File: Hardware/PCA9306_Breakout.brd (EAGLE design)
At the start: 17.8 x 10.2 mm, 15 parts

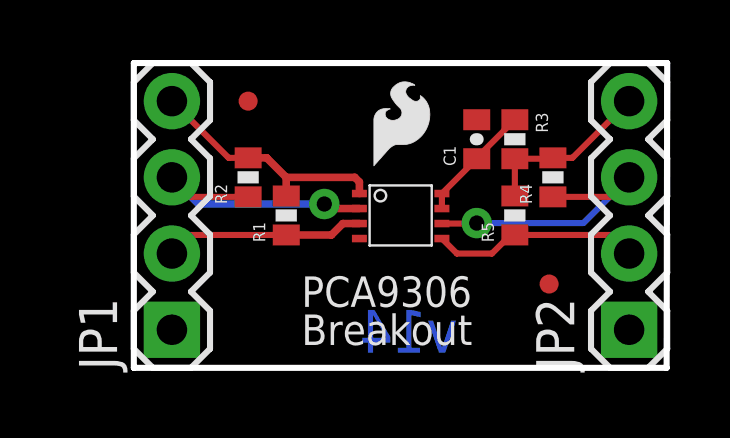
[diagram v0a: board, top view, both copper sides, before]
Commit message: Rerouted traces away from IC and changed packages to 0603. Add labels to the schematic on the header pins.
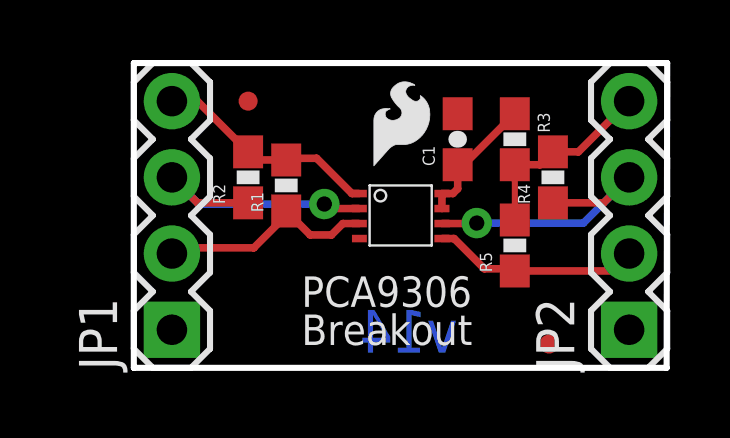
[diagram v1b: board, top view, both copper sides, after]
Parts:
- C1: device SparkFun:0402-CAP -> SparkFun:0603-CAP
- R1, R2, R3, R4, R5: device SparkFun:0402-RES -> SparkFun:0603-RES
- moved JP8 2.00 mm to (13.8, 0.79)
- moved FRAME1 1.80 mm to (-4.94, -10.2)
- moved R1 1.00 mm to (5.08, 6.08)
- moved R5 1.00 mm to (12.7, 4.08)
- moved C1 0.63 mm to (10.8, 7.62)
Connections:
- new net VREF_2: JP2.4, R3.2, R4.2, R5.2
- net VREF2: no longer JP2.4, R3.2, R4.2, R5.2
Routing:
- net VREF_2: track 0.00 -> 6.53 mm
- net VREF2: track 9.81 -> 4.50 mm
- net SDA2: track 7.84 -> 6.93 mm
- net VREF1: track 8.37 -> 7.57 mm
- net SDA1: track 6.66 -> 7.41 mm
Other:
- board text added: "T. Klopfenstein"
- board text removed: "M. Hord, T. Klopfenstein"

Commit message: Updating layout
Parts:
- moved R5 1.91 mm to (14.6, 4.08)
- moved R4 1.42 mm to (14.6, 7.62)
- moved R2 0.57 mm to (3.30, 6.10)
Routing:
- net GND: track 0.00 -> 7.88 mm
- net VREF2: track 4.50 -> 5.61 mm
- net SCL2: track 9.77 -> 8.96 mm
- net VREF_2: track 6.53 -> 7.34 mm
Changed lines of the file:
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@@
 <wire x1="0" y1="10.16" x2="0" y2="0" width="0.2032" layer="20"/>
 <wire x1="2.794" y1="11.049" x2="2.794" y2="-2.286" width="0.0254" layer="22"/>
-<wire x1="14.986" y1="11.557" x2="14.986" y2="-1.778" width="0.0254" layer="22"/>
+<wire x1="14.986" y1="10.922" x2="14.986" y2="-2.413" width="0.0254" layer="22"/>
 <wire x1="1.27" y1="8.89" x2="1.27" y2="1.27" width="0.254" layer="49"/>
 <wire x1="16.51" y1="8.89" x2="16.51" y2="1.27" width="0.254" layer="49"/>
@@
 <text x="10.795" y="0.508" size="1.4224" layer="16" font="vector" ratio="15" rot="MR0">v14</text>
 <text x="25.4" y="-10.16" size="1.778" layer="27" font="vector" ratio="15">T. Klopfenstein</text>
+<rectangle x1="7.3025" y1="3.81" x2="7.62" y2="4.1275" layer="41"/>
 </plain>
 <attributes>
@@
 <element name="U$1" library="miscellany" package="PSOP-8" value="PCA9306" x="8.89" y="5.08" rot="R270"/>
 <element name="R1" library="SparkFun" package="0603-RES" value="1k" x="5.08" y="6.08" rot="R90"/>
-<element name="R2" library="SparkFun" package="0603-RES" value="1k" x="3.81" y="6.35" rot="R90"/>
+<element name="R2" library="SparkFun" package="0603-RES" value="1k" x="3.302" y="6.096" rot="R90"/>
 <element name="R3" library="SparkFun" package="0603-RES" value="200k" x="12.7" y="7.62" rot="R270"/>
-<element name="R4" library="SparkFun" package="0603-RES" value="1k" x="13.97" y="6.35" rot="R90"/>
-<element name="R5" library="SparkFun" package="0603-RES" value="1k" x="12.7" y="4.08" rot="R90"/>
+<element name="R4" library="SparkFun" package="0603-RES" value="1k" x="14.605" y="7.62" rot="R90"/>
+<element name="R5" library="SparkFun" package="0603-RES" value="1k" x="14.605" y="4.08" rot="R90"/>
 <element name="C1" library="SparkFun" package="0603-CAP" value="0.1uF" x="10.795" y="7.62" rot="R90"/>
 <element name="JP1" library="SparkFun" package="1X04" value="" x="1.27" y="1.27" rot="R90"/>
@@
 <contactref element="JP1" pad="4"/>
 <wire x1="1.27" y1="8.89" x2="2.12" y2="8.89" width="0.254" layer="1"/>
-<wire x1="2.12" y1="8.89" x2="3.81" y2="7.2" width="0.254" layer="1"/>
+<wire x1="2.12" y1="8.89" x2="3.302" y2="6.946" width="0.254" layer="1"/>
 <wire x1="5.08" y1="6.93" x2="4.08" y2="6.93" width="0.254" layer="1"/>
-<wire x1="4.08" y1="6.93" x2="3.81" y2="7.2" width="0.254" layer="1"/>
+<wire x1="4.08" y1="6.93" x2="3.302" y2="6.946" width="0.254" layer="1"/>
 <wire x1="7.52" y1="5.81" x2="7.271" y2="5.81" width="0.254" layer="1"/>
 <wire x1="7.271" y1="5.81" x2="6.096" y2="6.985" width="0.254" layer="1"/>
@@
 <wire x1="1.27" y1="6.35" x2="2.159" y2="5.461" width="0.254" layer="16"/>
 <via x="6.35" y="5.461" extent="1-16" drill="0.508"/>
-<wire x1="3.81" y1="5.5" x2="2.12" y2="5.5" width="0.254" layer="1"/>
-<wire x1="2.12" y1="5.5" x2="1.27" y2="6.35" width="0.254" layer="1"/>
+<wire x1="3.302" y1="5.246" x2="2.374" y2="5.246" width="0.254" layer="1"/>
+<wire x1="2.374" y1="5.246" x2="1.27" y2="6.35" width="0.254" layer="1"/>
 </signal>
 <signal name="SDA1">
@@
 <vertex x="0" y="0"/>
 </polygon>
+<wire x1="7.52" y1="4.31" x2="7.1675" y2="4.31" width="0.254" layer="1"/>
+<wire x1="7.1675" y1="4.31" x2="6.6675" y2="3.81" width="0.254" layer="1"/>
+<wire x1="6.6675" y1="3.81" x2="6.35" y2="3.81" width="0.254" layer="1"/>
+<wire x1="6.35" y1="3.81" x2="6.35" y2="3.175" width="0.254" layer="1"/>
+<wire x1="6.35" y1="3.175" x2="4.445" y2="1.27" width="0.254" layer="1"/>
+<wire x1="4.445" y1="1.27" x2="1.27" y2="1.27" width="0.254" layer="1"/>
 </signal>
 <signal name="VREF2">
@@
 <wire x1="11" y1="6.77" x2="12.7" y2="8.47" width="0.254" layer="1"/>
 <contactref element="U$1" pad="8"/>
-<wire x1="10.27" y1="5.81" x2="10.27" y2="5.31" width="0.254" layer="1"/>
-<wire x1="10.27" y1="5.81" x2="10.636" y2="5.81" width="0.254" layer="1"/>
-<wire x1="10.636" y1="5.81" x2="10.795" y2="5.969" width="0.254" layer="1"/>
-<wire x1="10.795" y1="5.969" x2="10.795" y2="6.77" width="0.254" layer="1"/>
+<wire x1="10.27" y1="5.81" x2="10.954" y2="5.81" width="0.254" layer="1"/>
+<wire x1="10.27" y1="5.31" x2="10.771" y2="5.31" width="0.254" layer="1"/>
+<wire x1="10.771" y1="5.31" x2="11.049" y2="5.588" width="0.254" layer="1"/>
+<wire x1="11.049" y1="5.588" x2="11.049" y2="5.715" width="0.254" layer="1"/>
+<wire x1="11.049" y1="5.715" x2="11.049" y2="6.516" width="0.254" layer="1"/>
+<wire x1="11.049" y1="6.516" x2="10.795" y2="6.77" width="0.254" layer="1"/>
+<wire x1="10.954" y1="5.81" x2="11.049" y2="5.715" width="0.254" layer="1"/>
 </signal>
 <signal name="SCL2">
@@
 <contactref element="R4" pad="1"/>
 <contactref element="JP2" pad="3"/>
-<via x="11.43" y="4.826" extent="1-16" drill="0.508"/>
-<wire x1="13.97" y1="5.5" x2="15.66" y2="5.5" width="0.254" layer="1"/>
-<wire x1="15.66" y1="5.5" x2="16.51" y2="6.35" width="0.254" layer="1"/>
-<wire x1="10.27" y1="4.81" x2="11.414" y2="4.81" width="0.254" layer="1"/>
-<wire x1="11.414" y1="4.81" x2="11.43" y2="4.826" width="0.254" layer="1"/>
-<wire x1="11.43" y1="4.826" x2="14.986" y2="4.826" width="0.254" layer="16"/>
+<via x="12.7" y="4.826" extent="1-16" drill="0.508"/>
+<wire x1="12.7" y1="4.826" x2="14.986" y2="4.826" width="0.254" layer="16"/>
 <wire x1="14.986" y1="4.826" x2="16.51" y2="6.35" width="0.254" layer="16"/>
+<wire x1="14.605" y1="6.77" x2="16.09" y2="6.77" width="0.254" layer="1"/>
+<wire x1="16.09" y1="6.77" x2="16.51" y2="6.35" width="0.254" layer="1"/>
+<wire x1="10.27" y1="4.81" x2="12.684" y2="4.81" width="0.254" layer="1"/>
+<wire x1="12.684" y1="4.81" x2="12.7" y2="4.826" width="0.254" layer="1"/>
 </signal>
 <signal name="SDA2">
@@
 <contactref element="R5" pad="1"/>
 <contactref element="JP2" pad="2"/>
-<wire x1="12.7" y1="3.23" x2="15.93" y2="3.23" width="0.254" layer="1"/>
+<wire x1="14.605" y1="3.23" x2="15.93" y2="3.23" width="0.254" layer="1"/>
 <wire x1="15.93" y1="3.23" x2="16.51" y2="3.81" width="0.254" layer="1"/>
 <wire x1="10.27" y1="4.31" x2="10.676" y2="4.31" width="0.254" layer="1"/>
-<wire x1="10.676" y1="4.31" x2="11.684" y2="3.302" width="0.254" layer="1"/>
-<wire x1="11.684" y1="3.302" x2="12.628" y2="3.302" width="0.254" layer="1"/>
-<wire x1="12.628" y1="3.302" x2="12.7" y2="3.23" width="0.254" layer="1"/>
+<wire x1="10.676" y1="4.31" x2="11.756" y2="3.23" width="0.254" layer="1"/>
+<wire x1="14.605" y1="3.23" x2="11.756" y2="3.23" width="0.254" layer="1"/>
 </signal>
 <signal name="VREF_2">
@@
 <contactref element="R3" pad="2"/>
 <contactref element="JP2" pad="4"/>
-<wire x1="12.7" y1="6.77" x2="12.7" y2="4.93" width="0.2032" layer="1"/>
-<wire x1="13.97" y1="7.2" x2="14.82" y2="7.2" width="0.254" layer="1"/>
-<wire x1="14.82" y1="7.2" x2="16.51" y2="8.89" width="0.254" layer="1"/>
-<wire x1="12.7" y1="6.77" x2="13.54" y2="6.77" width="0.254" layer="1"/>
-<wire x1="13.54" y1="6.77" x2="13.97" y2="7.2" width="0.254" layer="1"/>
+<wire x1="12.7" y1="6.77" x2="14.605" y2="4.93" width="0.2032" layer="1"/>
+<wire x1="12.7" y1="6.77" x2="12.905" y2="6.77" width="0.254" layer="1"/>
+<wire x1="12.905" y1="6.77" x2="14.605" y2="8.47" width="0.254" layer="1"/>
+<wire x1="14.605" y1="8.47" x2="16.09" y2="8.47" width="0.254" layer="1"/>
+<wire x1="16.09" y1="8.47" x2="16.51" y2="8.89" width="0.254" layer="1"/>
 </signal>
 <signal name="NC">

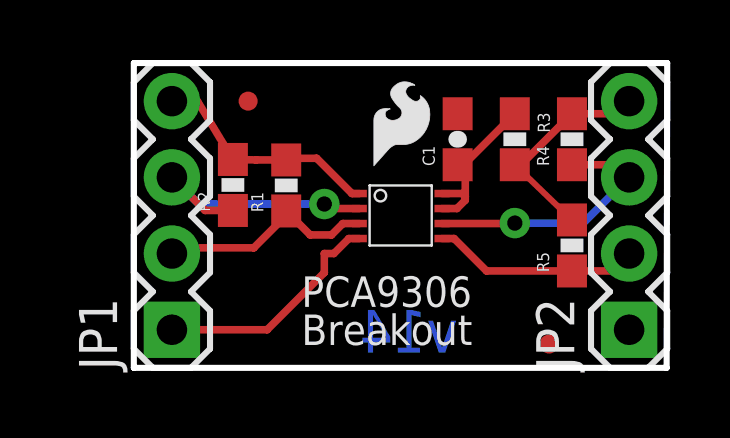
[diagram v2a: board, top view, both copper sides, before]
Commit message: Checking 1:1 FP on IC
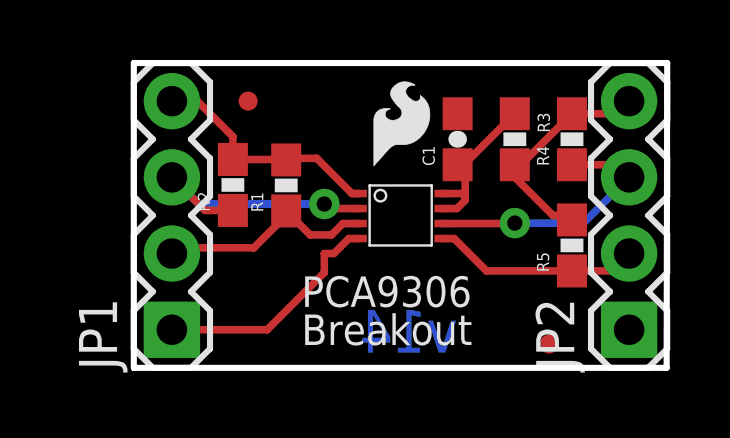
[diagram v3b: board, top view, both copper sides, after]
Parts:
- U$1: value PCA9306 -> (none); device miscellany:PSOP-8 -> SparkFun-DigitalIC:PSOP-8
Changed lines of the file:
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@@
 <layer number="106" name="bPlate" color="7" fill="1" visible="no" active="yes"/>
 <layer number="107" name="Crop" color="7" fill="1" visible="no" active="yes"/>
+<layer number="108" name="tplace-old" color="10" fill="1" visible="yes" active="yes"/>
+<layer number="109" name="ref-old" color="11" fill="1" visible="yes" active="yes"/>
 <layer number="116" name="Patch_BOT" color="9" fill="4" visible="no" active="yes"/>
 <layer number="121" name="_tsilk" color="7" fill="1" visible="no" active="yes"/>
@@
 </class>
 </classes>
-<designrules name="SparkFun">
+<designrules name="SparkFun *">
 <description language="en">&lt;b&gt;EAGLE Design Rules&lt;/b&gt;
 &lt;p&gt;
@@
 <param name="dpGapFactor" value="2.5"/>
 <param name="checkGrid" value="0"/>
-<param name="checkAngle" value="0"/>
+<param name="checkAngle" value="1"/>
 <param name="checkFont" value="1"/>
 <param name="checkRestrict" value="1"/>
@@
 </autorouter>
 <elements>
-<element name="U$1" library="miscellany" package="PSOP-8" value="PCA9306" x="8.89" y="5.08" rot="R270"/>
+<element name="U$1" library="SparkFun-DigitalIC" package="PSOP-8" value="" x="8.89" y="5.08" rot="R270">
+<attribute name="PROD_ID" value="IC-10023" x="8.89" y="5.08" size="1.778" layer="27" rot="R270" display="off"/>
+</element>
 <element name="R1" library="SparkFun" package="0603-RES" value="1k" x="5.08" y="6.08" rot="R90"/>
 <element name="R2" library="SparkFun" package="0603-RES" value="1k" x="3.302" y="6.096" rot="R90"/>
@@
 <contactref element="JP1" pad="4"/>
 <wire x1="1.27" y1="8.89" x2="2.12" y2="8.89" width="0.254" layer="1"/>
-<wire x1="2.12" y1="8.89" x2="3.302" y2="6.946" width="0.254" layer="1"/>
-<wire x1="5.08" y1="6.93" x2="4.08" y2="6.93" width="0.254" layer="1"/>
-<wire x1="4.08" y1="6.93" x2="3.302" y2="6.946" width="0.254" layer="1"/>
 <wire x1="7.52" y1="5.81" x2="7.271" y2="5.81" width="0.254" layer="1"/>
 <wire x1="7.271" y1="5.81" x2="6.096" y2="6.985" width="0.254" layer="1"/>
 <wire x1="6.096" y1="6.985" x2="5.135" y2="6.985" width="0.254" layer="1"/>
 <wire x1="5.135" y1="6.985" x2="5.08" y2="6.93" width="0.254" layer="1"/>
+<wire x1="2.12" y1="8.89" x2="3.302" y2="7.708" width="0.254" layer="1"/>
+<wire x1="3.302" y1="7.708" x2="3.302" y2="6.946" width="0.254" layer="1"/>
+<wire x1="5.08" y1="6.93" x2="5.064" y2="6.946" width="0.254" layer="1"/>
+<wire x1="5.064" y1="6.946" x2="3.302" y2="6.946" width="0.254" layer="1"/>
 </signal>
 <signal name="SCL1">
@@
 <contactref element="R3" pad="2"/>
 <contactref element="JP2" pad="4"/>
-<wire x1="12.7" y1="6.77" x2="14.605" y2="4.93" width="0.2032" layer="1"/>
 <wire x1="12.7" y1="6.77" x2="12.905" y2="6.77" width="0.254" layer="1"/>
 <wire x1="12.905" y1="6.77" x2="14.605" y2="8.47" width="0.254" layer="1"/>
 <wire x1="14.605" y1="8.47" x2="16.09" y2="8.47" width="0.254" layer="1"/>
 <wire x1="16.09" y1="8.47" x2="16.51" y2="8.89" width="0.254" layer="1"/>
+<wire x1="14.605" y1="4.93" x2="14.455" y2="5.08" width="0.254" layer="1"/>
+<wire x1="14.455" y1="5.08" x2="13.97" y2="5.08" width="0.254" layer="1"/>
+<wire x1="13.97" y1="5.08" x2="12.7" y2="6.35" width="0.254" layer="1"/>
+<wire x1="12.7" y1="6.35" x2="12.7" y2="6.77" width="0.254" layer="1"/>
 </signal>
 <signal name="NC">
